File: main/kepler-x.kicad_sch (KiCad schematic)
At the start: 169 parts, among them IC1 SLG46826G, J1 HDMI_C_1.3, J10 Conn_01x04, J11 Micro_SD_Card_Det_Hirose_DM3AT, J12 Filter Sel, J13 Conn_01x02_Pin, J14 Conn_01x02_Pin, J2 Conn_01x02_Pin, J3 MIDI OUT, J4 Raspberry Pi, J5 AudioJack3, J6 MIDI IN, J7 Conn_01x02_Pin, J8 Conn_02x05_Odd_Even, J9 Conn_01x02_Pin, Q1 2SA1162GR, Q2 2SA1162GR, Q3 2SC2712-GR, Q4 2SC2712-GR, Q5 2SC2712-GR, Q6 2SC2712-GR, SW1 SW_DPDT_x2, SW3 SW_DIP_x02, U1 Bus-X68000-ext, U10 74LVCR162245, U11 WM8804GEDS{slash}RV, U12 TC7MPB9307F, U13 TC7MPB9307F, U14 P0082(DE0-NANO), U15 PLR135-T10, U16 PCM5102A, U17 XC6201P332MR-G, U18 H11L1, U19 TC7MPB9307F, U2 LM1117GS-3.3, U20 TC7MPB9307F, U21 XC6201P332MR-G, U22 PCA9515DP, U23 74LVC541A, U24 CH32V003F4P6, U3 INA3221AIRGVR, U4 74LVC16374A, U5 74LVC16374A, U6 74LVC16374A, U7 74LVC16374A, U8 74LVC16374A, U9 74LVC16374A, X1 ASV-24.576MHz, Y1 XJHCELNANF-12MHZ

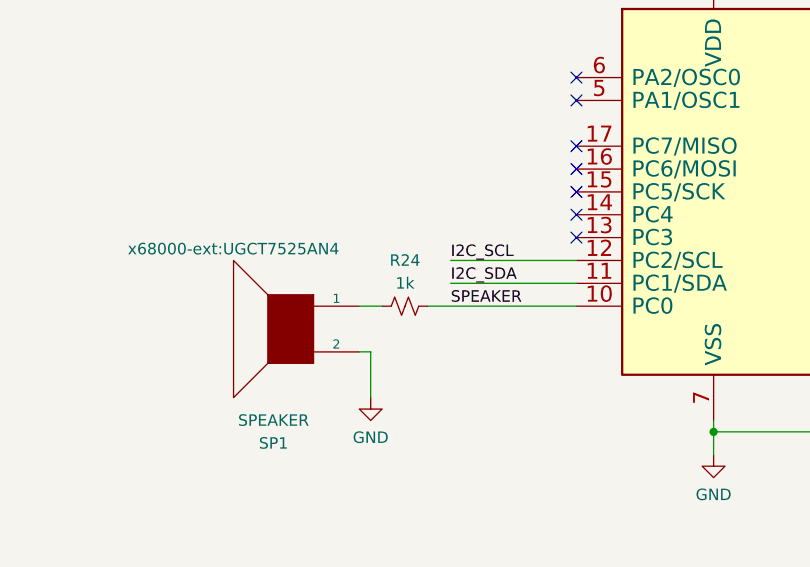
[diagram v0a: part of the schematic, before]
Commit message: v1.0.1 - Changed one of the two sets of open jumper pairs to a bridged jumper
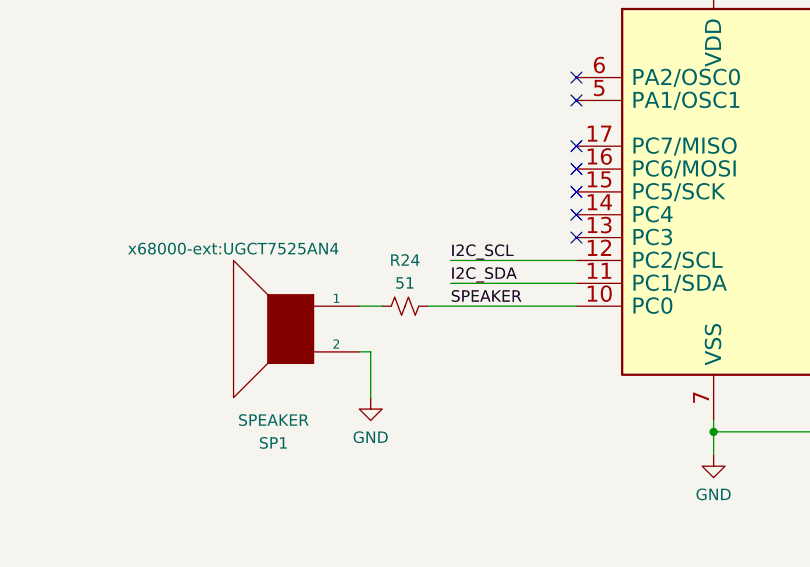
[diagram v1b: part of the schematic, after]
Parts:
- R24: value 1k -> 51
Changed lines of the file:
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@@
       (effects (font (size 1.27 1.27)))
     )
-    (property "Value" "1k" (at 618.49 245.11 90)
+    (property "Value" "51" (at 618.49 245.11 90)
       (effects (font (size 1.27 1.27)))
     )

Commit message: Llast commit ussing TSSOP20 package for CH32V003
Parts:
- removed R24: 51, Resistor_SMD:R_0603_1608Metric_Pad0.98x0.95mm_HandSolder, symbol Device:R_Small_US
- removed SW1: SW_DPDT_x2, x68000-ext:MST22D18G2-SlideSwitch-DPDT, symbol Switch:SW_DPDT_x2
- removed U14: P0082(DE0-NANO), x68000-ext:MODULE_P0082_TOPMOUNT, symbol x68000-ext:P0082(DE0-NANO)
- added C39, C40, C41, C42, C43, C44, C45, C46, C47, C48: 0.1uF, Capacitor_SMD:C_0603_1608Metric_Pad1.08x0.95mm_HandSolder, symbol Device:C_Small
- added C49: 10uF, Capacitor_Tantalum_SMD:CP_EIA-3216-18_Kemet-A, symbol Device:C_Polarized_Small_US
- added D11: SS2040FL, Diode_SMD:D_SOD-123F, symbol Device:D_Schottky_Small
- added J15, J16: Conn_01x03_Pin, Connector_PinHeader_2.54mm:PinHeader_1x03_P2.54mm_Vertical, symbol Connector:Conn_01x03_Pin
- added Q7: 2SC2712-GR, x68000-ext:SC-59_Handsoldering, symbol Device:Q_NPN_BEC
- added R33: 1M, Resistor_SMD:R_0603_1608Metric_Pad0.98x0.95mm_HandSolder, symbol Device:R_Small_US
- added R34: 10k, Resistor_SMD:R_0603_1608Metric_Pad0.98x0.95mm_HandSolder, symbol Device:R_Small_US
- added U25: P0082(DE0-NANO)_JP1, x68000-ext:MODULE_P0082_TOPMOUNT_JP1, symbol x68000-ext:P0082(DE0-NANO)_JP1
- added U26: P0082(DE0-NANO)_JP2, x68000-ext:MODULE_P0082_TOPMOUNT_JP2, symbol x68000-ext:P0082(DE0-NANO)_JP2
- D1, D12, D2, D6, D7, D9: footprint Diode_SMD:D_1206_3216Metric_Pad1.42x1.75mm_HandSolder -> Diode_SMD:D_SOD-123F
- FB1, FB2, FB3: footprint Inductor_SMD:L_0805_2012Metric_Pad1.15x1.40mm_HandSolder -> Inductor_SMD:L_0603_1608Metric_Pad1.05x0.95mm_HandSolder
- H1, H2, H3, H4, J12, JP1, JP10, JP11, JP2, JP4, JP5, JP6, JP8, JP9, TP1, TP2, TP3, TP4, TP5, TP6, TP7, TP8, U1: now left out of the parts list
- J10: now not fitted
- J2, J7: now not fitted; now left out of the parts list
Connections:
- net +3.3V: now also SP1.1, C39.1, C40.1, C41.1, C42.1, C43.1, C44.1, C45.1, C46.1, C47.1, C48.1, D11.1 (K), R34.1
- net BUS_MODE0: now also U25.JP1_20 (GPIO_015)
- net BUS_MODE1: now also U25.JP1_19 (GPIO_014)
- net BUS_MODE2: now also U25.JP1_18 (GPIO_013)
- net BUS_MODE3: now also U25.JP1_17 (GPIO_012)
- net ENABLE_MMC_n: now also R34.2
- net ExEXRESET: now also R33.2
- net ExIACK2: now also J16.1 (Pin_1)
- net ExIACK4: now also J16.3 (Pin_3)
- net ExIRQ2: now also J15.1 (Pin_1)
- net ExIRQ4: now also J15.3 (Pin_3)
- net GND: now also C39.2, C40.2, C41.2, C42.2, C43.2, C44.2, C45.2, C46.2, C47.2, C48.2, C49.2, Q7.2 (E), U25.JP1_12 (GPIO-0_GND), U25.JP1_30 (GPIO-0_GND), U25.S1 (SHIELD), U25.S2 (SHIELD), U25.S3 (SHIELD), U25.S4 (SHIELD), U26.JP2_12 (GPIO-1_GND), U26.JP2_30 (GPIO-1_GND); no longer SP1.2
- net HDMI_CLKn: now also U25.JP1_16 (GPIO_011)
- net HDMI_CLKp: now also U25.JP1_15 (GPIO_010)
- net HDMI_D0n: now also U25.JP1_13 (GPIO_08)
- net HDMI_D0p: now also U25.JP1_10 (GPIO_07)
- net HDMI_D1n: now also U25.JP1_9 (GPIO_06)
- net HDMI_D1p: now also U25.JP1_8 (GPIO_05)
- net HDMI_D2n: now also U25.JP1_5 (GPIO_02)
- net HDMI_D2p: now also U25.JP1_6 (GPIO_03)
- net I2C_SCL: now also U25.JP1_7 (GPIO_04)
- net I2C_SDA: now also U25.JP1_14 (GPIO_09)
- net I2S_BCLK_FROM_PI: now also U26.JP2_36 (GPIO_129)
- net I2S_DATA_FROM_PI: now also U26.JP2_37 (GPIO_130)
- net I2S_DATA_IN: now also U25.JP1_25 (GPIO_020)
- net I2S_LRCK_FROM_PI: now also U26.JP2_35 (GPIO_128)
- net MIDI_IN: now also U26.JP2_39 (GPIO_132)
- net MIDI_OUT: now also U26.JP2_40 (GPIO_133)
- net MIDI_OUT_TO_PI: now also U26.JP2_34 (GPIO_127)
- net MMC_CS: now also U26.JP2_32 (GPIO_125)
- net MMC_MISO: now also U26.JP2_31 (GPIO_124)
- net MMC_MOSI: now also U26.JP2_28 (GPIO_123)
- net MMC_SCK: now also U26.JP2_27 (GPIO_122)
- net RasPi_SPI_CS0: now also U25.JP1_3 (GPIO_0_IN1)
- net RasPi_SPI_MISO: now also U25.JP1_4 (GPIO_01)
- net RasPi_SPI_MOSI: now also U25.JP1_2 (GPIO_00)
- net RasPi_SPI_SCLK: now also U25.JP1_1 (GPIO_0_IN0)
- net SPEAKER: now also Q7.1 (B)
- net SWIO: now also U26.JP2_33 (GPIO_126)
- net VCC: now also C49.1, R33.1
- net iAS: now also U25.JP1_26 (GPIO_021)
- net iBG: now also U26.JP2_8 (GPIO_15)
- net iBGACK: now also U25.JP1_40 (GPIO_033)
- net iBR: now also U25.JP1_39 (GPIO_032)
- net iCLK10M: now also U26.JP2_1 (GPIO_1_IN0)
- net iCLK24M576: now also U26.JP2_3 (GPIO_1_IN1)
- net iDONE: now also U25.JP1_33 (GPIO_026)
- net iDTACK: now also U25.JP1_34 (GPIO_027)
- net iDTC: now also U26.JP2_5 (GPIO_12)
- net iEXACK: now also U26.JP2_6 (GPIO_13)
- net iEXOWN: now also U25.JP1_37 (GPIO_030)
- net iEXPCL: now also U25.JP1_36 (GPIO_029)
- net iEXREQ: now also U25.JP1_35 (GPIO_028)
- net iEXRESET: now also U26.JP2_38 (GPIO_131)
- net iHSYNC: now also U26.JP2_4 (GPIO_11)
- net iIACK: now also U26.JP2_7 (GPIO_14)
- net iIDDIR: now also U25.JP1_32 (GPIO_025)
- net iIRQ: now also U25.JP1_38 (GPIO_031)
- net iLDS: now also U25.JP1_27 (GPIO_022)
- net iRW: now also U25.JP1_31 (GPIO_024)
- net iSB0: now also U26.JP2_9 (GPIO_16)
- net iSB1: now also U26.JP2_10 (GPIO_17)
- net iSB10: now also U26.JP2_21 (GPIO_116)
- net iSB11: now also U26.JP2_22 (GPIO_117)
- net iSB12: now also U26.JP2_23 (GPIO_118)
- net iSB13: now also U26.JP2_24 (GPIO_119)
- net iSB14: now also U26.JP2_25 (GPIO_120)
- net iSB15: now also U26.JP2_26 (GPIO_121)
- net iSB2: now also U26.JP2_13 (GPIO_18)
- net iSB3: now also U26.JP2_14 (GPIO_19)
- net iSB4: now also U26.JP2_15 (GPIO_110)
- net iSB5: now also U26.JP2_16 (GPIO_111)
- net iSB6: now also U26.JP2_17 (GPIO_112)
- net iSB7: now also U26.JP2_18 (GPIO_113)
- net iSB8: now also U26.JP2_19 (GPIO_114)
- net iSB9: now also U26.JP2_20 (GPIO_115)
- net iUDS: now also U25.JP1_28 (GPIO_023)
- net iVSYNC: now also U26.JP2_2 (GPIO_10)
- net at TP8.1: now also U25.JP1_29 (GPIO-0_VCC3P3)
- net at U12.16 (B3), U19.13 (B6): now also J15.2 (Pin_2)
- net at R20.2: now also U25.JP1_21 (GPIO_016)
- net at D12.2 (A), D2.1 (K): now also U26.JP2_11 (GPIO-1_VCC_SYS)
- net at U10.12 (1B8): now also J16.2 (Pin_2)
- net at TP7.1: now also U25.JP1_11 (GPIO-0_VCC_SYS)
- net at R22.1: now also U25.JP1_22 (GPIO_017)
- net at R21.2: now also U25.JP1_23 (GPIO_018)
- net at R23.1: now also U25.JP1_24 (GPIO_019)
- net at JP9.3 (B): now also U26.JP2_29 (GPIO-1_VCC3P3)
- new net: D11.2 (A), Q7.3 (C), SP1.2
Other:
- moved on the sheet: C14, C15, C16, C35, SP1

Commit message: V3.0.1
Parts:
- removed U24: CH32V003F4P6, Package_SO:TSSOP-20_4.4x6.5mm_P0.65mm, symbol x68000-ext:CH32V003A4M6
- added U14: CH32V003F4U6, Package_DFN_QFN:QFN-20-1EP_3x3mm_P0.4mm_EP1.65x1.65mm_ThermalVias, symbol x68000-ext:CH32V003F4U6
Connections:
- net +3.3V: now also U14.6 (VDD)
- net ENABLE_MMC_n: now also U14.1 (PD7)
- net GND: now also U14.21 (VSS), U14.4 (VSS)
- net I2C_SCL: now also U14.9 (PC2/SCL)
- net I2C_SDA: now also U14.8 (PC1/SDA)
- net KEPLERX_STATUS_LED: now also U14.20 (PD6)
- net MMC_ACCESS_LED: now also U14.19 (PD5)
- net MMC_CS: now also U14.17 (PD3)
- net MMC_DET_n: now also U14.18 (PD4)
- net SPEAKER: now also U14.7 (PC0)
- net SWIO: now also U14.15 (PD1/SWIO)
- net WM8804_INTn: now also U14.16 (PD2)
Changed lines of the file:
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@@
     (stroke (width 0) (type default))
   )
+  (wire (pts (xy 647.7 260.35) (xy 647.7 261.62))
+    (stroke (width 0) (type default))
+  )
   (wire (pts (xy 208.28 565.15) (xy 208.28 516.89))
     (stroke (width 0) (type default))
@@
     (stroke (width 0) (type default))
   )
+  (wire (pts (xy 647.7 261.62) (xy 652.78 261.62))
+    (stroke (width 0) (type default))
+  )
   (wire (pts (xy 269.24 342.9) (xy 269.24 340.36))
     (stroke (width 0) (type default))
@@
     )
   )
+  (symbol (lib_id "x68000-ext:CH32V003F4U6") (at 652.78 234.95 0) (unit 1)
+    (in_bom yes) (on_board yes) (dnp no) (fields_autoplaced)
+    (property "Reference" "U14" (at 655.3234 209.55 0)
+      (effects (font (size 1.524 1.524)) (justify left))
+    )
+    (property "Value" "CH32V003F4U6" (at 655.3234 212.09 0)
+      (effects (font (size 1.524 1.524)) (justify left))
+    )
+    (property "Footprint" "Package_DFN_QFN:QFN-20-1EP_3x3mm_P0.4mm_EP1.65x1.65mm_ThermalVias" (at 681.99 261.62 0)
+      (effects (font (size 1.524 1.524)) hide)
+    )
+    (property "Datasheet" "" (at 589.28 257.81 0)
+      (effects (font (size 1.524 1.524)) hide)
+    )
+    (property "LCSC" "C5299908" (at 652.78 234.95 0)
+      (effects (font (size 1.27 1.27)) hide)
+    )
+    (pin "1")
+    (pin "10")
+    (pin "11")
+    (pin "12")
+    (pin "13")
+    (pin "14")
+    (pin "15")
+    (pin "16")
+    (pin "17")
+    (pin "18")
+    (pin "19")
+    (pin "2")
+    (pin "20")
+    (pin "21")
+    (pin "3")
+    (pin "4")
+    (pin "5")
+    (pin "6")
+    (pin "7")
+    (pin "8")
+    (pin "9")
+    (instances
+      (project "kepler-x"
+        (path "/5e579fe7-5bb7-49e5-ac0c-de4dc8db9d3d"
+          (reference "U14") (unit 1)
+        )
+      )
+    )
+  )
   (symbol (lib_id "power:VCC") (at 746.76 229.87 0) (unit 1)
     (in_bom yes) (on_board yes) (dnp no) (fields_autoplaced)
@@
         )
       )
-    )
-  )
-  (symbol (lib_id "x68000-ext:CH32V003A4M6") (at 652.78 234.95 0) (unit 1)
-    (in_bom yes) (on_board yes) (dnp no) (fields_autoplaced)
-    (property "Reference" "U24" (at 655.3234 210.185 0)
-      (effects (font (size 1.524 1.524)) (justify left))
-    )
-    (property "Value" "CH32V003F4P6" (at 655.3234 212.725 0)
-      (effects (font (size 1.524 1.524)) (justify left))
-    )
-    (property "Footprint" "Package_SO:TSSOP-20_4.4x6.5mm_P0.65mm" (at 681.99 261.62 0)
-      (effects (font (size 1.524 1.524)) hide)
-    )
-    (property "Datasheet" "" (at 589.28 257.81 0)
-      (effects (font (size 1.524 1.524)) hide)
-    )
-    (pin "1")
-    (pin "10")
-    (pin "11")
-    (pin "12")
-    (pin "13")
-    (pin "14")
-    (pin "15")
-    (pin "16")
-    (pin "17")
-    (pin "18")
-    (pin "19")
-    (pin "2")
-    (pin "20")
-    (pin "3")
-    (pin "4")
-    (pin "5")
-    (pin "6")
-    (pin "7")
-    (pin "8")
-    (pin "9")
-    (instances
-      (project "kepler-x"
-        (path "/5e579fe7-5bb7-49e5-ac0c-de4dc8db9d3d"
-          (reference "U24") (unit 1)
-        )
-      )
